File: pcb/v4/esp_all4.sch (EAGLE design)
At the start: 31 parts, among them IC1 4000D, Q1 BUZ11BH

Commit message: added v4, with i2c
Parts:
- added R2, R3: 4.7k, rcl:R-EU_M0805
- added SV4: (no value), con-lstb:MA04-1
- renumbered DIMMING to T_DIM1, DIMMING1 to T_DIM2, DIMMING2 to T_DIM3, U$12 to DP3, U$13 to DP2
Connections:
- removed net DHT_SIG: DHT22.DAT, ESP.D4
- removed net NOT: ESP.D3, IC1A.I1
- new net DHT_SIG/SDA: DHT22.DAT, ESP.D4, SV4.2
- new net N$3: R2.2, R3.2, T_DIM3.D
- new net SCL: ESP.D5, SV4.1
- net DIMMING3: now also R3.1; no longer T_DIM3.D
- net GND: now also R2.1, SV4.3
- net PIR: now also ESP.D3; no longer ESP.D5
- net VDD: now also SV4.4

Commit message: fixed LDO
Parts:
- LDO: value REG1118 -> REG1117; device burr-brown:REG1118 -> burr-brown:REG1117
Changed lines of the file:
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@@
 <part name="U$11" library="JKW_CHIP" deviceset="LOGO_10X10_SILK" device=""/>
 <part name="D3" library="diode" deviceset="ES2D" device=""/>
-<part name="LDO" library="burr-brown" deviceset="REG1118" device=""/>
+<part name="LDO" library="burr-brown" deviceset="REG1117" device=""/>
 <part name="Q1" library="transistor-power" deviceset="BUZ11" device="BH"/>
 <part name="GND11" library="supply1" deviceset="GND" device=""/>

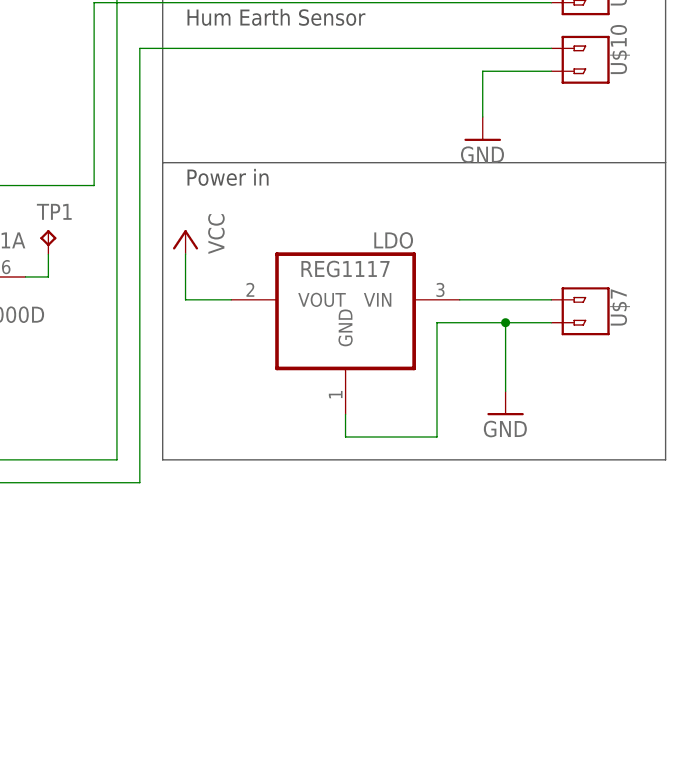
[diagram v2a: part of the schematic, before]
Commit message: added voltage reg
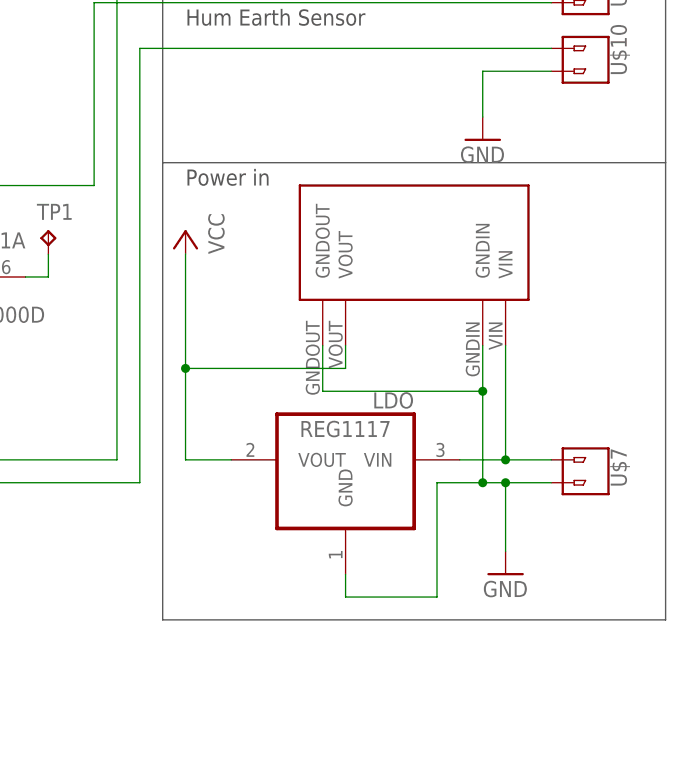
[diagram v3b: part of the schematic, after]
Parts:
- added U$12: MP1584EN_FRAMELESS, JKW_CHIP:MP1584EN_FRAMELESS
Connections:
- net GND: now also U$12.GNDIN, U$12.GNDOUT
- net N$17: now also U$12.VIN
- net VCC: now also U$12.VOUT
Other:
- moved on the sheet: LDO, U$7
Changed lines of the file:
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@@
 <?xml version="1.0" encoding="utf-8"?>
 <!DOCTYPE eagle SYSTEM "eagle.dtd">
-<eagle version="7.6.0">
+<eagle version="7.7.0">
 <drawing>
 <settings>
@@
 <part name="GND15" library="supply1" deviceset="GND" device=""/>
 <part name="VDD8" library="supply1" deviceset="VDD" device=""/>
+<part name="U$12" library="JKW_CHIP" deviceset="MP1584EN_FRAMELESS" device=""/>
 </parts>
 <sheets>
@@
 <text x="167.64" y="88.9" size="1.778" layer="97">Hum Earth Sensor</text>
 <wire x1="165.1" y1="73.66" x2="220.98" y2="73.66" width="0.1524" layer="97"/>
-<wire x1="220.98" y1="73.66" x2="220.98" y2="40.64" width="0.1524" layer="97"/>
-<wire x1="220.98" y1="40.64" x2="165.1" y2="40.64" width="0.1524" layer="97"/>
-<wire x1="165.1" y1="40.64" x2="165.1" y2="73.66" width="0.1524" layer="97"/>
+<wire x1="220.98" y1="73.66" x2="220.98" y2="22.86" width="0.1524" layer="97"/>
+<wire x1="220.98" y1="22.86" x2="165.1" y2="22.86" width="0.1524" layer="97"/>
+<wire x1="165.1" y1="22.86" x2="165.1" y2="73.66" width="0.1524" layer="97"/>
 <text x="167.64" y="71.12" size="1.778" layer="97">Power in</text>
 <text x="15.24" y="88.9" size="1.778" layer="97" rot="R90">Option for 3V from ESP (default)</text>
@@
 <attribute name="NAME" x="-2.54" y="71.501" size="1.778" layer="95"/>
 </instance>
-<instance part="U$7" gate="G$1" x="208.28" y="55.88" smashed="yes">
-<attribute name="NAME" x="216.662" y="55.372" size="1.778" layer="95" rot="R90"/>
+<instance part="U$7" gate="G$1" x="208.28" y="38.1" smashed="yes">
+<attribute name="NAME" x="216.662" y="37.592" size="1.778" layer="95" rot="R90"/>
 </instance>
 <instance part="P+1" gate="VCC" x="167.64" y="66.04" rot="MR0"/>
-<instance part="GND4" gate="1" x="203.2" y="45.72"/>
+<instance part="GND4" gate="1" x="203.2" y="27.94"/>
 <instance part="P+2" gate="VCC" x="33.02" y="35.56" rot="MR0"/>
 <instance part="P+3" gate="VCC" x="5.08" y="81.28" rot="MR0"/>
@@
 <instance part="U$11" gate="G$1" x="-25.4" y="157.48"/>
 <instance part="D3" gate="G$1" x="40.64" y="40.64" rot="R270"/>
-<instance part="LDO" gate="G$1" x="185.42" y="58.42" rot="MR0"/>
+<instance part="LDO" gate="G$1" x="185.42" y="40.64" rot="MR0"/>
 <instance part="Q1" gate="1" x="114.3" y="106.68" smashed="yes">
 <attribute name="NAME" x="116.84" y="106.68" size="1.778" layer="95"/>
@@
 <instance part="GND15" gate="1" x="22.86" y="12.7"/>
 <instance part="VDD8" gate="G$1" x="22.86" y="33.02"/>
+<instance part="U$12" gate="G$1" x="205.74" y="58.42" rot="MR0"/>
 </instances>
 <busses>
@@
 <pinref part="U$7" gate="G$1" pin="2"/>
 <pinref part="GND4" gate="1" pin="GND"/>
-<wire x1="208.28" y1="55.88" x2="203.2" y2="55.88" width="0.1524" layer="91"/>
-<wire x1="203.2" y1="55.88" x2="203.2" y2="48.26" width="0.1524" layer="91"/>
+<wire x1="208.28" y1="38.1" x2="203.2" y2="38.1" width="0.1524" layer="91"/>
+<wire x1="203.2" y1="38.1" x2="203.2" y2="30.48" width="0.1524" layer="91"/>
 <pinref part="LDO" gate="G$1" pin="GND"/>
-<wire x1="185.42" y1="45.72" x2="185.42" y2="43.18" width="0.1524" layer="91"/>
-<wire x1="185.42" y1="43.18" x2="195.58" y2="43.18" width="0.1524" layer="91"/>
-<wire x1="195.58" y1="43.18" x2="195.58" y2="55.88" width="0.1524" layer="91"/>
-<wire x1="195.58" y1="55.88" x2="203.2" y2="55.88" width="0.1524" layer="91"/>
-<junction x="203.2" y="55.88"/>
+<wire x1="185.42" y1="27.94" x2="185.42" y2="25.4" width="0.1524" layer="91"/>
+<wire x1="185.42" y1="25.4" x2="195.58" y2="25.4" width="0.1524" layer="91"/>
+<wire x1="195.58" y1="25.4" x2="195.58" y2="38.1" width="0.1524" layer="91"/>
+<wire x1="195.58" y1="38.1" x2="200.66" y2="38.1" width="0.1524" layer="91"/>
+<junction x="203.2" y="38.1"/>
+<pinref part="U$12" gate="G$1" pin="GNDIN"/>
+<wire x1="200.66" y1="38.1" x2="203.2" y2="38.1" width="0.1524" layer="91"/>
+<wire x1="200.66" y1="53.34" x2="200.66" y2="48.26" width="0.1524" layer="91"/>
+<pinref part="U$12" gate="G$1" pin="GNDOUT"/>
+<wire x1="200.66" y1="48.26" x2="200.66" y2="38.1" width="0.1524" layer="91"/>
+<wire x1="182.88" y1="53.34" x2="182.88" y2="48.26" width="0.1524" layer="91"/>
+<wire x1="182.88" y1="48.26" x2="200.66" y2="48.26" width="0.1524" layer="91"/>
+<junction x="200.66" y="48.26"/>
+<junction x="200.66" y="38.1"/>
 </segment>
 <segment>
@@
 <pinref part="P+1" gate="VCC" pin="VCC"/>
 <pinref part="LDO" gate="G$1" pin="VOUT"/>
-<wire x1="172.72" y1="58.42" x2="167.64" y2="58.42" width="0.1524" layer="91"/>
-<wire x1="167.64" y1="58.42" x2="167.64" y2="63.5" width="0.1524" layer="91"/>
+<wire x1="172.72" y1="40.64" x2="167.64" y2="40.64" width="0.1524" layer="91"/>
+<wire x1="167.64" y1="40.64" x2="167.64" y2="50.8" width="0.1524" layer="91"/>
+<pinref part="U$12" gate="G$1" pin="VOUT"/>
+<wire x1="167.64" y1="50.8" x2="167.64" y2="63.5" width="0.1524" layer="91"/>
+<wire x1="185.42" y1="53.34" x2="185.42" y2="50.8" width="0.1524" layer="91"/>
+<wire x1="185.42" y1="50.8" x2="167.64" y2="50.8" width="0.1524" layer="91"/>
+<junction x="167.64" y="50.8"/>
 </segment>
 <segment>
@@
 <segment>
 <pinref part="U$7" gate="G$1" pin="1"/>
-<wire x1="208.28" y1="58.42" x2="198.12" y2="58.42" width="0.1524" layer="91"/>
+<wire x1="208.28" y1="40.64" x2="203.2" y2="40.64" width="0.1524" layer="91"/>
 <pinref part="LDO" gate="G$1" pin="VIN"/>
-</segment>
-</net>
+<pinref part="U$12" gate="G$1" pin="VIN"/>
+<wire x1="203.2" y1="40.64" x2="198.12" y2="40.64" width="0.1524" layer="91"/>
+<wire x1="203.2" y1="53.34" x2="203.2" y2="40.64" width="0.1524" layer="91"/>
+<junction x="203.2" y="40.64"/>
+</segment>
+</net>
